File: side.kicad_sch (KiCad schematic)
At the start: 74 parts, among them J1 Conn_01x02_Pin, J2 HRO_TYPE-C-31-M-14, J3 Battery, J9 TC2030_SWD, Q2 2N7002, SW1 PWR, SW2 RST, U1 SRV05-4, U10 MAX17048, U3 BQ24075, U8 nRF52840_moko_mk08

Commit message: progress
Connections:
- net ALERT: no longer names the net of U10.5 (~{ALRT})
- net UG_EN: no longer names the net of U8.49 (P1.00)
- net UG_LV: no longer names the net of U8.31 (P0.22)
- no-connect marks 17 -> 50

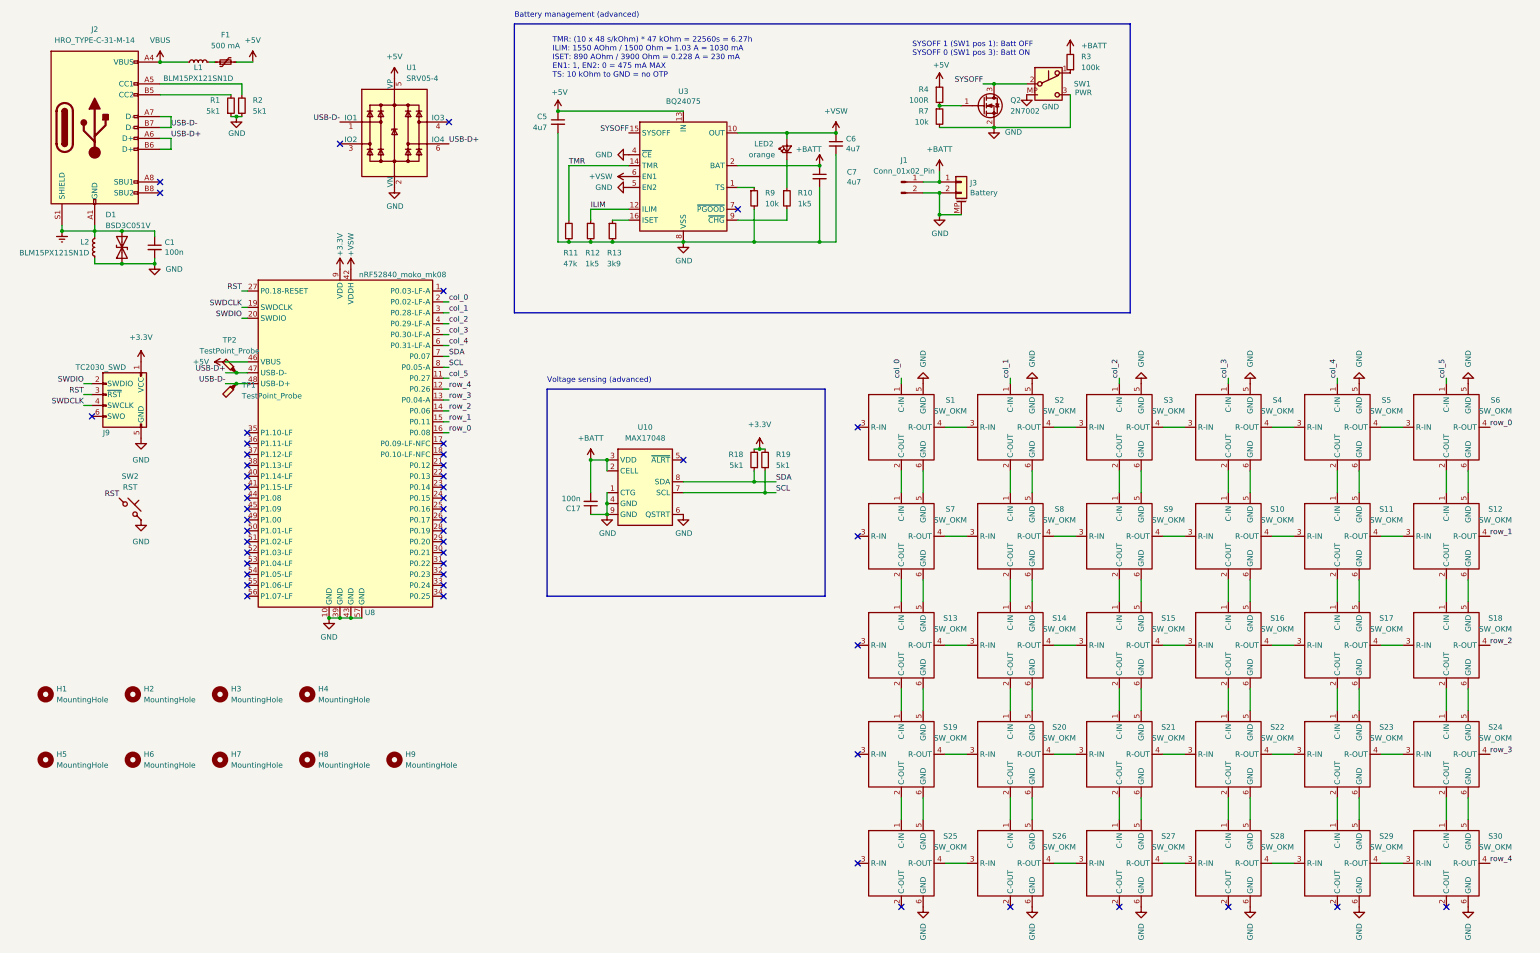
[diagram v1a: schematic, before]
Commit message: migration to KiCad 10
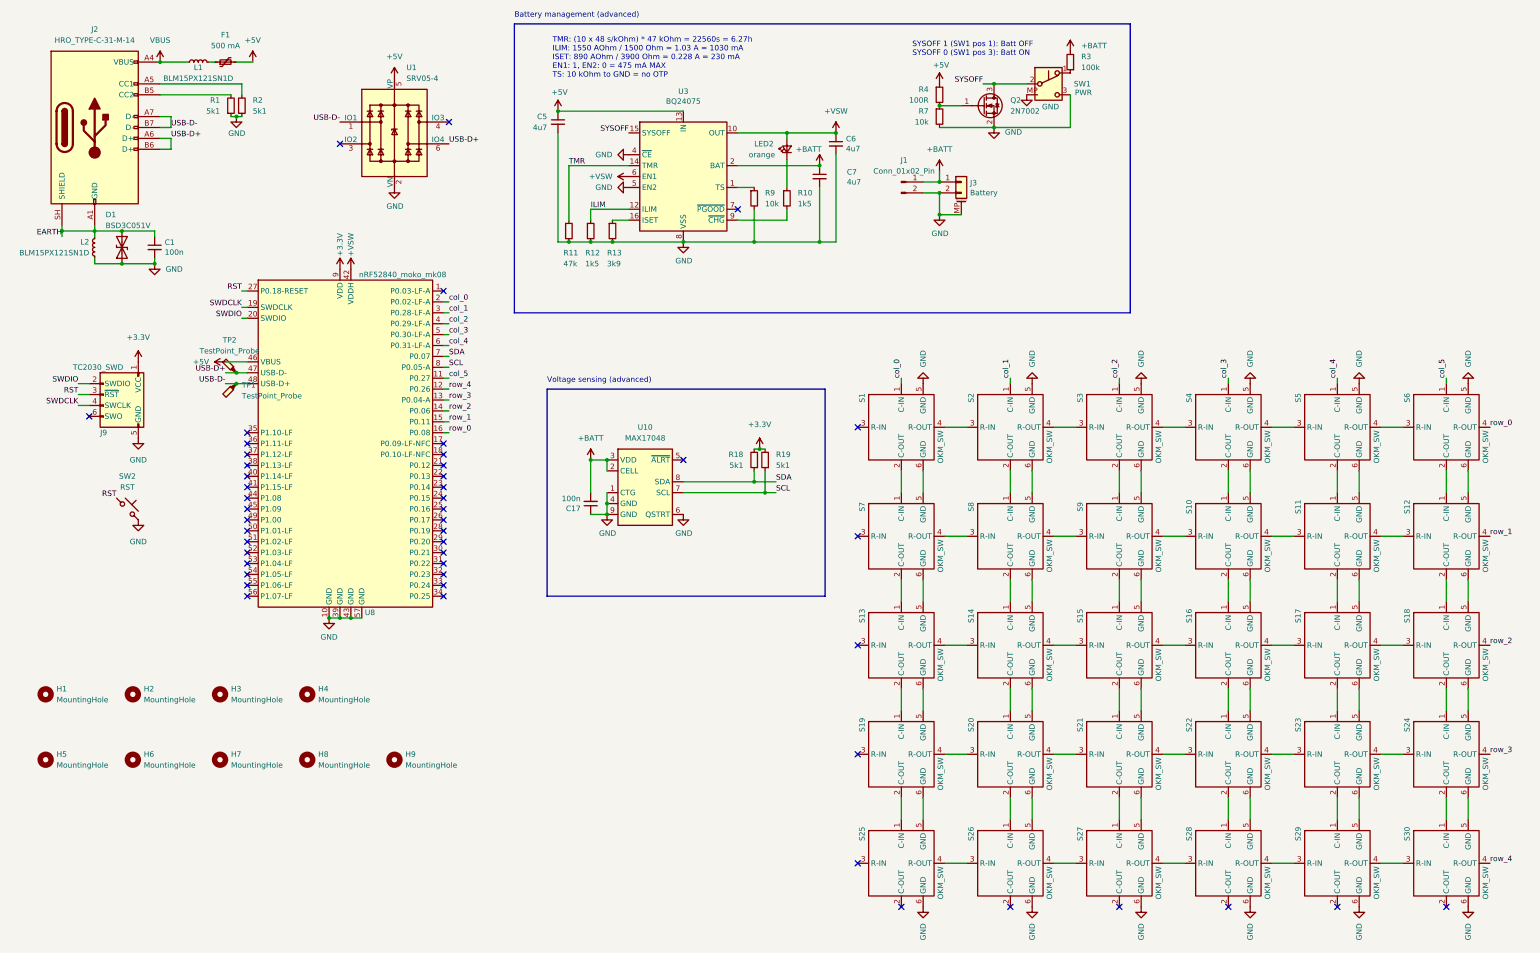
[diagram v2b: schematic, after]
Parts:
- H1, H2, H3, H4, H5, H6, H7, H8, H9: footprint Graz_Footprints:MountingHole_M2_Graz -> kigraz:MHOLE_M2
- J1: footprint Graz_Footprints:Generic_Battery_Connector -> kigraz:BATT_CONN_SMD
- J2: symbol Connector:USB_C_Receptacle_USB2.0 -> Connector:USB_C_Receptacle_USB2.0_14P
- S1, S10, S11, S12, S13, S14, S15, S16, S17, S18, S19, S2, S20, S21, S22, S23, S24, S25, S26, S27, S28, S29, S3, S30, S4, S5, S6, S7, S8, S9: value SW_OKM -> OKM_SW; footprint Graz_Footprints:One Key Module Graz -> kigraz:OKM_SW; symbol 0_graz_symbols:SW_OKM -> kigraz:OKM_SW
- SW1: footprint Graz_Footprints:SW_SSSS811101 -> kigraz:ALPS_SPDT_SW; symbol Switch:SW_Push_SPDT -> kigraz:SW_Push_SPDT
- U10: footprint Graz_Footprints:DFN-8-1EP_2x2mm_P0.5mm_EP0.7x1.3mm -> kigraz:DFN-8-1EP_2x2mm_P0.5mm_EP0.7x1.3mm; symbol marbastlib-various:MAX17048 -> PCM_marbastlib-various:MAX17048
- U8: footprint Graz_Footprints:nRF52840_moko_mk08_GRAZ -> kigraz:MOKO_MK08
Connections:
- net Earth renamed EARTH
- net EARTH: now also J2.SH (SHIELD); no longer J2.S1 (SHIELD)
- no-connect marks 50 -> 48
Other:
- moved on the sheet: J9, SW2

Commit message: bom rules
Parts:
- S1, S10, S11, S12, S13, S14, S15, S16, S17, S18, S19, S2, S20, S21, S22, S23, S24, S25, S26, S27, S28, S29, S3, S30, S4, S5, S6, S7, S8, S9, TP1, TP2: now left out of the parts list
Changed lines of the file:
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@@
 		(body_style 1)
 		(exclude_from_sim no)
-		(in_bom yes)
+		(in_bom no)
 		(on_board yes)
 		(in_pos_files yes)
@@
 		(body_style 1)
 		(exclude_from_sim no)
-		(in_bom yes)
+		(in_bom no)
 		(on_board yes)
 		(in_pos_files yes)
@@
 		(body_style 1)
 		(exclude_from_sim no)
-		(in_bom yes)
+		(in_bom no)
 		(on_board yes)
 		(in_pos_files yes)
@@
 		(body_style 1)
 		(exclude_from_sim no)
-		(in_bom yes)
+		(in_bom no)
 		(on_board yes)
 		(in_pos_files yes)
@@
 		(body_style 1)
 		(exclude_from_sim no)
-		(in_bom yes)
+		(in_bom no)
 		(on_board yes)
 		(in_pos_files yes)
@@
 		(body_style 1)
 		(exclude_from_sim no)
-		(in_bom yes)
+		(in_bom no)
 		(on_board yes)
 		(in_pos_files yes)
@@
 		(body_style 1)
 		(exclude_from_sim no)
-		(in_bom yes)
+		(in_bom no)
 		(on_board yes)
 		(in_pos_files yes)
@@
 		(body_style 1)
 		(exclude_from_sim no)
-		(in_bom yes)
+		(in_bom no)
 		(on_board yes)
 		(in_pos_files yes)
@@
 		(body_style 1)
 		(exclude_from_sim no)
-		(in_bom yes)
+		(in_bom no)
 		(on_board yes)
 		(in_pos_files yes)
@@
 		(body_style 1)
 		(exclude_from_sim no)
-		(in_bom yes)
+		(in_bom no)
 		(on_board yes)
 		(in_pos_files yes)
@@
 		(body_style 1)
 		(exclude_from_sim no)
-		(in_bom yes)
+		(in_bom no)
 		(on_board yes)
 		(in_pos_files yes)
@@
 		(body_style 1)
 		(exclude_from_sim no)
-		(in_bom yes)
+		(in_bom no)
 		(on_board yes)
 		(in_pos_files yes)
@@
 		(body_style 1)
 		(exclude_from_sim no)
-		(in_bom yes)
+		(in_bom no)
 		(on_board yes)
 		(in_pos_files yes)
@@
 		(body_style 1)
 		(exclude_from_sim no)
-		(in_bom yes)
+		(in_bom no)
 		(on_board yes)
 		(in_pos_files yes)
@@
 		(body_style 1)
 		(exclude_from_sim no)
-		(in_bom yes)
+		(in_bom no)
 		(on_board yes)
 		(in_pos_files yes)
@@
 		(body_style 1)
 		(exclude_from_sim no)
-		(in_bom yes)
+		(in_bom no)
 		(on_board yes)
 		(in_pos_files yes)
@@
 		(body_style 1)
 		(exclude_from_sim no)
-		(in_bom yes)
+		(in_bom no)
 		(on_board yes)
 		(in_pos_files yes)
@@
 		(body_style 1)
 		(exclude_from_sim no)
-		(in_bom yes)
+		(in_bom no)
 		(on_board yes)
 		(in_pos_files yes)
@@
 		(body_style 1)
 		(exclude_from_sim no)
-		(in_bom yes)
+		(in_bom no)
 		(on_board yes)
 		(in_pos_files yes)
@@
 		(body_style 1)
 		(exclude_from_sim no)
-		(in_bom yes)
+		(in_bom no)
 		(on_board yes)
 		(in_pos_files yes)
@@
 		(body_style 1)
 		(exclude_from_sim no)
-		(in_bom yes)
+		(in_bom no)
 		(on_board yes)
 		(in_pos_files yes)
@@
 		(body_style 1)
 		(exclude_from_sim no)
-		(in_bom yes)
+		(in_bom no)
 		(on_board yes)
 		(in_pos_files yes)
@@
 		(body_style 1)
 		(exclude_from_sim no)
-		(in_bom yes)
+		(in_bom no)
 		(on_board yes)
 		(in_pos_files yes)
@@
 		(body_style 1)
 		(exclude_from_sim no)
-		(in_bom yes)
+		(in_bom no)
 		(on_board yes)
 		(in_pos_files yes)
@@
 		(body_style 1)
 		(exclude_from_sim no)
-		(in_bom yes)
+		(in_bom no)
 		(on_board yes)
 		(in_pos_files yes)
@@
 		(body_style 1)
 		(exclude_from_sim no)
-		(in_bom yes)
+		(in_bom no)
 		(on_board yes)
 		(in_pos_files yes)
@@
 		(body_style 1)
 		(exclude_from_sim no)
-		(in_bom yes)
+		(in_bom no)
 		(on_board yes)
 		(in_pos_files yes)
@@
 		(body_style 1)
 		(exclude_from_sim no)
-		(in_bom yes)
+		(in_bom no)
 		(on_board yes)
 		(in_pos_files yes)
@@
 		(body_style 1)
 		(exclude_from_sim no)
-		(in_bom yes)
+		(in_bom no)
 		(on_board yes)
 		(in_pos_files yes)
@@
 		(body_style 1)
 		(exclude_from_sim no)
-		(in_bom yes)
+		(in_bom no)
 		(on_board yes)
 		(in_pos_files yes)
@@
 		(body_style 1)
 		(exclude_from_sim no)
-		(in_bom yes)
+		(in_bom no)
 		(on_board yes)
 		(in_pos_files yes)
@@
 		(body_style 1)
 		(exclude_from_sim no)
-		(in_bom yes)
+		(in_bom no)
 		(on_board yes)
 		(in_pos_files yes)

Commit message: rm aux batt conn from bom
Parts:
- J1: now left out of the parts list
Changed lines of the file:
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@@
 		(body_style 1)
 		(exclude_from_sim no)
-		(in_bom yes)
+		(in_bom no)
 		(on_board yes)
 		(in_pos_files yes)

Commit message: rm sw conn from bom
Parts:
- J9: now left out of the parts list
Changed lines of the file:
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@@
 		(body_style 1)
 		(exclude_from_sim no)
-		(in_bom yes)
+		(in_bom no)
 		(on_board yes)
 		(in_pos_files yes)

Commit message: post crash
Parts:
- added LED3: LT VH9G-Q2OO-25-1, LED_SMD:LED_0402_1005Metric, symbol Device:LED_Small
- added R25: 1k5, Resistor_SMD:R_0402_1005Metric, symbol Device:R_Small
- LED2: value orange -> LW QH8G-Q2OO-3K5L-1
- U8: now left out of the parts list
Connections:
- net +VSW: now also LED3.2 (A)
- net at U3.7 (~{PGOOD}): now also R25.2
- new net: LED3.1 (K), R25.1
- no-connect marks 48 -> 47
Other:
- moved on the sheet: C6, C7, J1, J3, LED2, R10, R9

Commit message: update VQFN-16-1EP_3x3mm_P0.5mm_EP1.6x1.6mm footprint
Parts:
- U3: footprint Package_DFN_QFN:VQFN-16-1EP_3x3mm_P0.5mm_EP1.6x1.6mm -> kigraz:VQFN-16-1EP_3x3mm_P0.5mm_EP1.6x1.6mm
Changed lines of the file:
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@@
 			)
 		)
-		(property "Footprint" "Package_DFN_QFN:VQFN-16-1EP_3x3mm_P0.5mm_EP1.6x1.6mm"
+		(property "Footprint" "kigraz:VQFN-16-1EP_3x3mm_P0.5mm_EP1.6x1.6mm"
 			(at 179.07 68.58 0)
 			(hide yes)

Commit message: Add new DFN fp with 0.22mm mask bridges for manu compat
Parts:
- U10: footprint kigraz:DFN-8-1EP_2x2mm_P0.5mm_EP0.7x1.3mm -> kigraz:DFN-8-1EP_2x2mm_P0.5mm_EP0.7x1.3mm_SM0.22mm
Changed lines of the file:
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@@
 			)
 		)
-		(property "Footprint" "kigraz:DFN-8-1EP_2x2mm_P0.5mm_EP0.7x1.3mm"
+		(property "Footprint" "kigraz:DFN-8-1EP_2x2mm_P0.5mm_EP0.7x1.3mm_SM0.22mm"
 			(at 153.035 137.16 0)
 			(hide yes)
